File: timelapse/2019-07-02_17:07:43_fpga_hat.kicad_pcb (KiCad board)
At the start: 4 copper layers, 65 x 56.5 mm, 90 parts, among them J1 2x20, J2 AudioJack3, J3 Conn_02x06_Top_Bottom, J4 Conn_02x06_Top_Bottom, J5 Conn_02x06_Top_Bottom, J6 Conn_01x02, SW1 PTS815, SW2 PTS815, SW3 PTS815, SW4 PTS815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

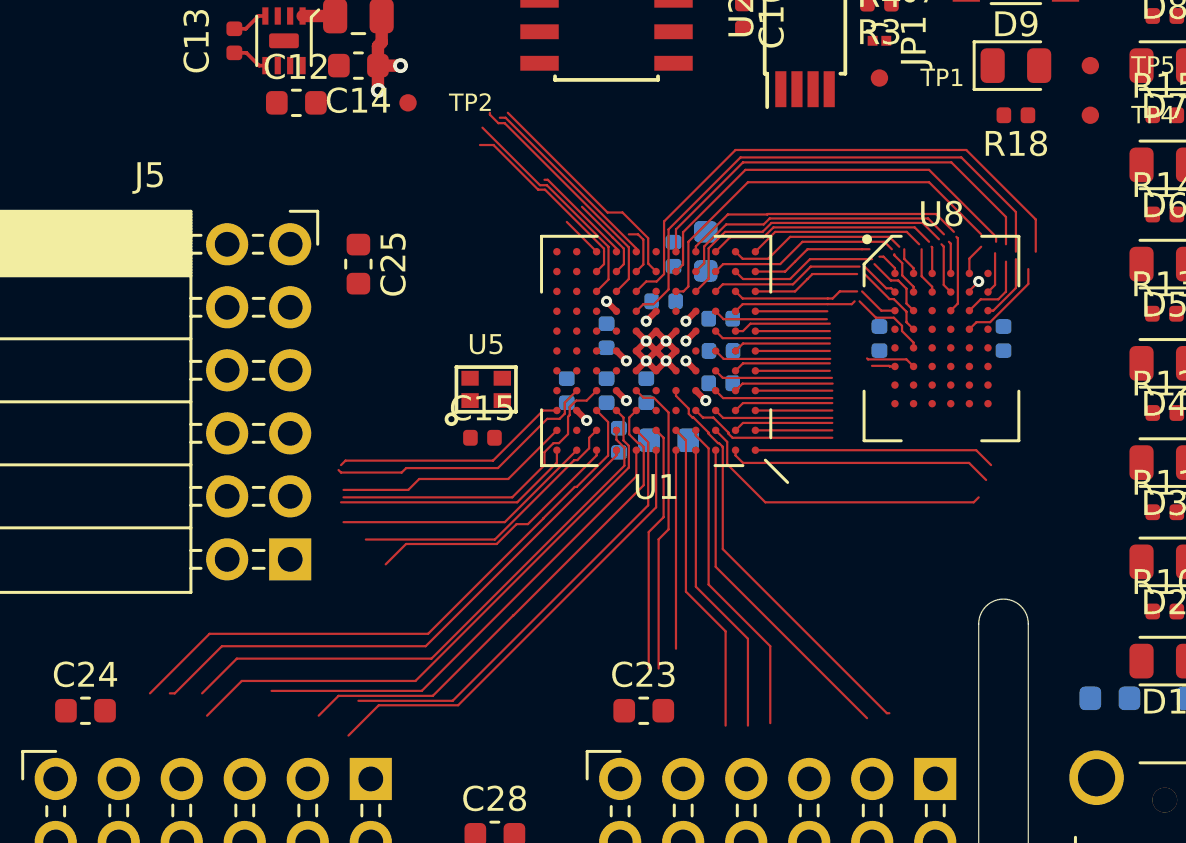
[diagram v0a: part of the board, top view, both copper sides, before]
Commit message: Continue FPGA escape. Start escaping SRAM.
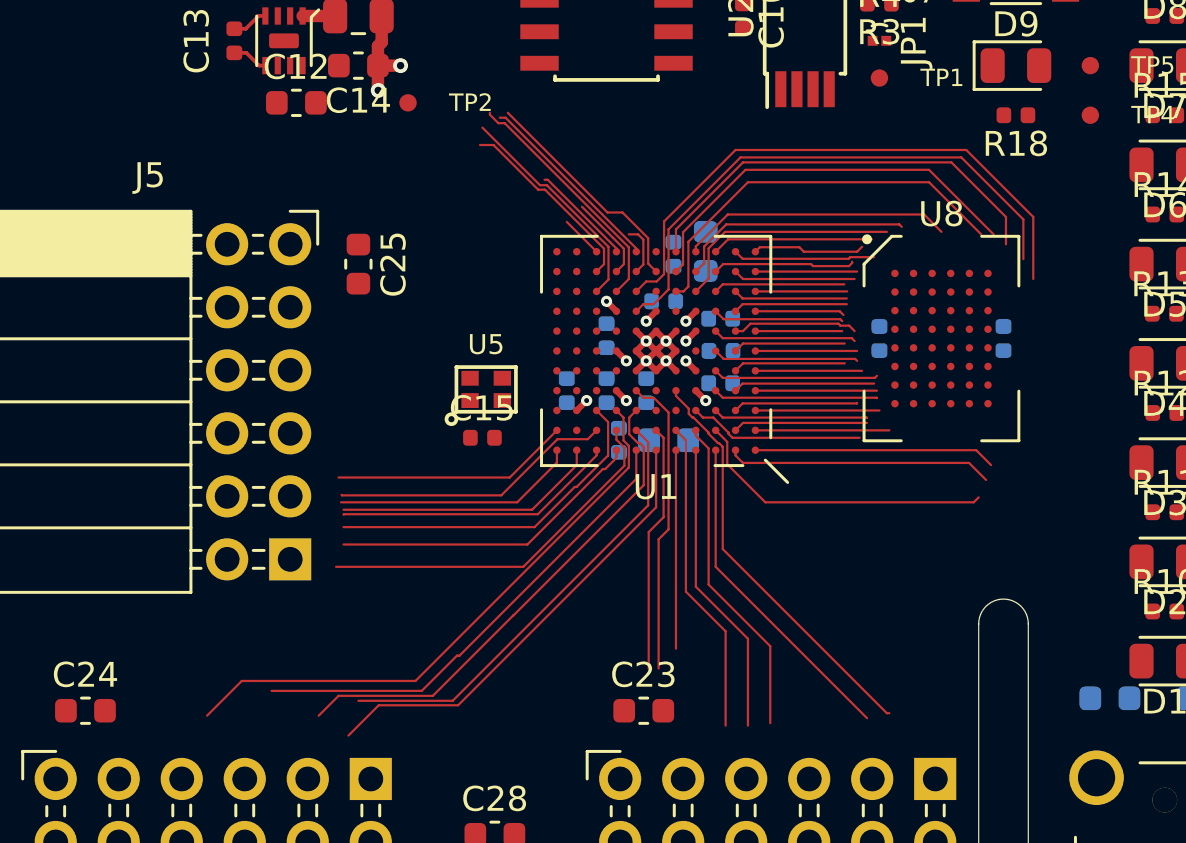
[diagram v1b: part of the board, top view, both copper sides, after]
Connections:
- U1 pad E3: /SRAM_A9 -> /SRAM_DQ11
- U1 pad F1: /SRAM_A0 -> /SRAM_DQ12
- U1 pad G1: /SRAM_DQ11 -> /SRAM_A9
- U1 pad G3: /SRAM_DQ12 -> /SRAM_A0
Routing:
- net /SW4: track 12.9 -> 0.00 mm
- net /SW7: track 11.3 -> 0.00 mm
- net /IO0_2: track 24.4 -> 13.9 mm
- net /GP14_UART_TXD: track 9.61 -> 0.00 mm
- net /IO1_0: track 22.2 -> 12.8 mm
- net /IO0_4: track 22.4 -> 14.9 mm
- net /SRAM_A6: track 9.07 -> 4.92 mm
- net /SRAM_DQ12: track 7.93 -> 4.10 mm
- net /SRAM_A4: track 6.47 -> 3.70 mm
- net /SRAM_A15: track 9.25 -> 6.51 mm
- net /SRAM_A10: track 7.14 -> 4.53 mm
- net /SRAM_A14: track 11.9 -> 9.41 mm
- net /SRAM_DQ3: track 8.56 -> 6.22 mm
- net /SRAM_A3: track 6.87 -> 4.60 mm
- net /SRAM_DQ10: track 6.63 -> 4.52 mm
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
